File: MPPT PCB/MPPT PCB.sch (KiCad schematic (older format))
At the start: 26 parts, among them J1 Conn_01x03_Male, J10 Conn_01x03_Male, J11 Conn_01x03_Male, J12 Conn_01x03_Male, J13 Conn_01x03_Male, J2 Conn_01x03_Male, J3 Conn_01x06_Female, J4 Conn_01x03_Male, J5 Screw_Terminal_01x02, J6 Conn_01x03_Male, J7 Conn_01x03_Male, J8 Screw_Terminal_01x02, J9 Conn_01x06_Female, P1 Conn_01x15_Female, P2 Conn_01x15_Female, SW1 SW_Push

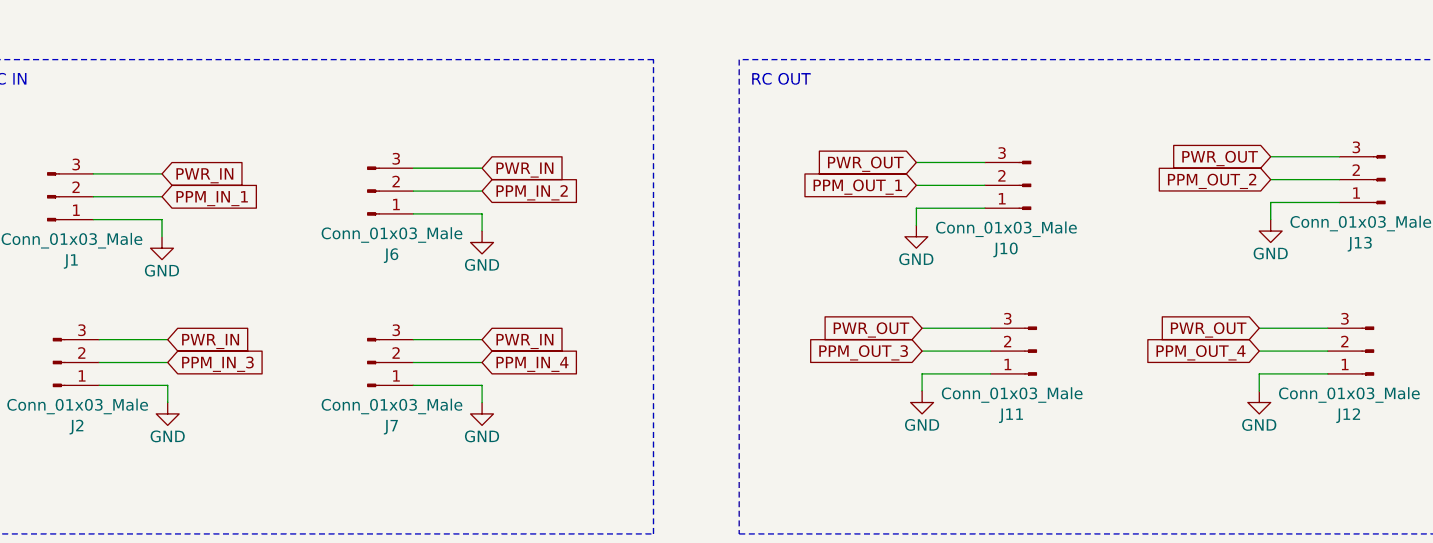
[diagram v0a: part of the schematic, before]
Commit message: Fixed servo pinout (Input and Output)
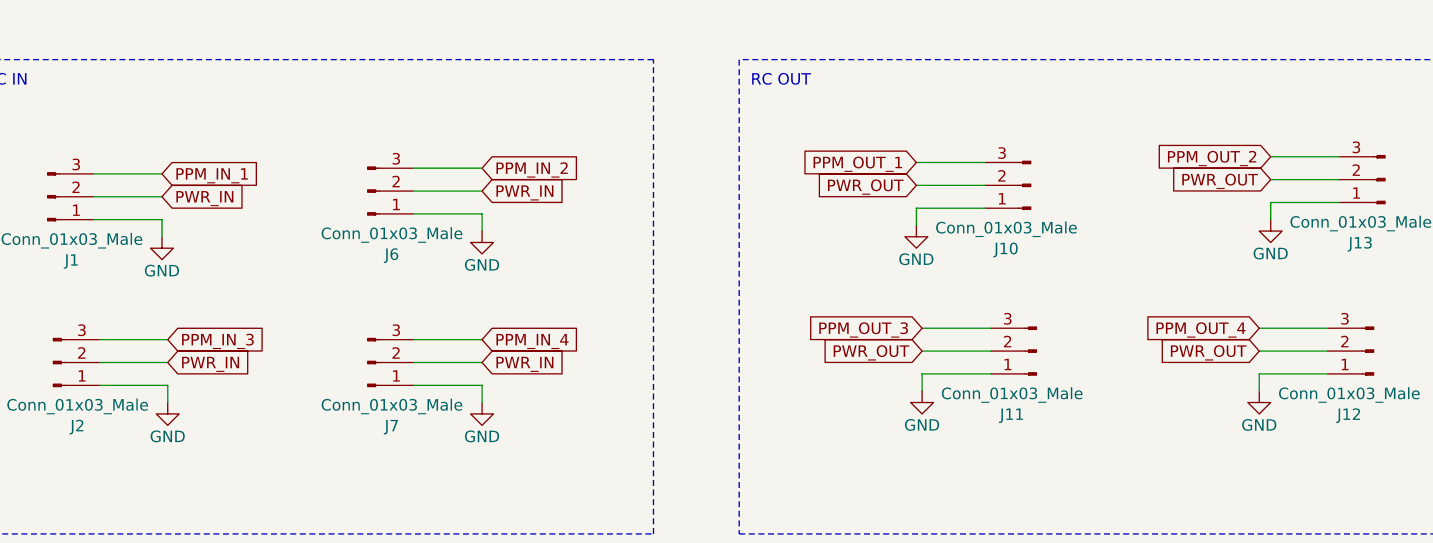
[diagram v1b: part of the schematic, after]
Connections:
- net PPM_IN_1: now also J1.3 (Pin_3); no longer J1.2 (Pin_2)
- net PPM_IN_2: now also J6.3 (Pin_3); no longer J6.2 (Pin_2)
- net PPM_IN_3: now also J2.3 (Pin_3); no longer J2.2 (Pin_2)
- net PPM_IN_4: now also J7.3 (Pin_3); no longer J7.2 (Pin_2)
- net PPM_OUT_1: now also J10.3 (Pin_3); no longer J10.2 (Pin_2)
- net PPM_OUT_2: now also J13.3 (Pin_3); no longer J13.2 (Pin_2)
- net PPM_OUT_3: now also J11.3 (Pin_3); no longer J11.2 (Pin_2)
- net PPM_OUT_4: now also J12.3 (Pin_3); no longer J12.2 (Pin_2)
- net PWR_IN: now also J1.2 (Pin_2), J2.2 (Pin_2), J6.2 (Pin_2), J7.2 (Pin_2); no longer J1.3 (Pin_3), J2.3 (Pin_3), J6.3 (Pin_3), J7.3 (Pin_3)
- net PWR_OUT: now also J10.2 (Pin_2), J11.2 (Pin_2), J12.2 (Pin_2), J13.2 (Pin_2); no longer J10.3 (Pin_3), J11.3 (Pin_3), J12.3 (Pin_3), J13.3 (Pin_3)
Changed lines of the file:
@@
 Title "MPPT solar board"
 Date "2019-10-12"
-Rev "r1"
+Rev "r2"
 Comp "Luis Miranda"
 Comment1 ""
@@
 	1    0    0    -1
 $EndComp
+Text GLabel 1650 1150 2    50   Input ~ 0
+PPM_IN_1
+Wire Wire Line
+	1650 1425 1650 1350
+Wire Wire Line
+	1650 1350 1350 1350
+Wire Wire Line
+	1650 1250 1350 1250
 Text GLabel 1650 1250 2    50   Input ~ 0
-PPM_IN_1
-Wire Wire Line
-	1650 1425 1650 1350
-Wire Wire Line
-	1650 1350 1350 1350
-Wire Wire Line
-	1650 1250 1350 1250
-Text GLabel 1650 1150 2    50   Input ~ 0
 PWR_IN
 Wire Wire Line
@@
 	1    0    0    -1
 $EndComp
+Text GLabel 1675 1875 2    50   Input ~ 0
+PPM_IN_3
+Wire Wire Line
+	1675 2150 1675 2075
+Wire Wire Line
+	1675 2075 1375 2075
+Wire Wire Line
+	1675 1975 1375 1975
 Text GLabel 1675 1975 2    50   Input ~ 0
-PPM_IN_3
-Wire Wire Line
-	1675 2150 1675 2075
-Wire Wire Line
-	1675 2075 1375 2075
-Wire Wire Line
-	1675 1975 1375 1975
-Text GLabel 1675 1875 2    50   Input ~ 0
 PWR_IN
 Wire Wire Line
@@
 	1    0    0    -1
 $EndComp
+Text GLabel 3050 1125 2    50   Input ~ 0
+PPM_IN_2
+Wire Wire Line
+	3050 1400 3050 1325
+Wire Wire Line
+	3050 1325 2750 1325
+Wire Wire Line
+	3050 1225 2750 1225
 Text GLabel 3050 1225 2    50   Input ~ 0
-PPM_IN_2
-Wire Wire Line
-	3050 1400 3050 1325
-Wire Wire Line
-	3050 1325 2750 1325
-Wire Wire Line
-	3050 1225 2750 1225
-Text GLabel 3050 1125 2    50   Input ~ 0
 PWR_IN
 Wire Wire Line
@@
 	1    0    0    -1
 $EndComp
+Text GLabel 3050 1875 2    50   Input ~ 0
+PPM_IN_4
+Wire Wire Line
+	3050 2150 3050 2075
+Wire Wire Line
+	3050 2075 2750 2075
+Wire Wire Line
+	3050 1975 2750 1975
 Text GLabel 3050 1975 2    50   Input ~ 0
-PPM_IN_4
-Wire Wire Line
-	3050 2150 3050 2075
-Wire Wire Line
-	3050 2075 2750 2075
-Wire Wire Line
-	3050 1975 2750 1975
-Text GLabel 3050 1875 2    50   Input ~ 0
 PWR_IN
 Wire Wire Line
@@
 	-1   0    0    -1
 $EndComp
+Text GLabel 4950 1100 0    50   Input ~ 0
+PPM_OUT_1
+Wire Wire Line
+	4950 1375 4950 1300
+Wire Wire Line
+	4950 1300 5250 1300
+Wire Wire Line
+	4950 1200 5250 1200
 Text GLabel 4950 1200 0    50   Input ~ 0
-PPM_OUT_1
-Wire Wire Line
-	4950 1375 4950 1300
-Wire Wire Line
-	4950 1300 5250 1300
-Wire Wire Line
-	4950 1200 5250 1200
-Text GLabel 4950 1100 0    50   Input ~ 0
 PWR_OUT
 Wire Wire Line
@@
 	-1   0    0    -1
 $EndComp
+Text GLabel 4975 1825 0    50   Input ~ 0
+PPM_OUT_3
+Wire Wire Line
+	4975 2100 4975 2025
+Wire Wire Line
+	4975 2025 5275 2025
+Wire Wire Line
+	4975 1925 5275 1925
 Text GLabel 4975 1925 0    50   Input ~ 0
-PPM_OUT_3
-Wire Wire Line
-	4975 2100 4975 2025
-Wire Wire Line
-	4975 2025 5275 2025
-Wire Wire Line
-	4975 1925 5275 1925
-Text GLabel 4975 1825 0    50   Input ~ 0
 PWR_OUT
 Wire Wire Line
@@
 	-1   0    0    -1
 $EndComp
+Text GLabel 6500 1075 0    50   Input ~ 0
+PPM_OUT_2
+Wire Wire Line
+	6500 1350 6500 1275
+Wire Wire Line
+	6500 1275 6800 1275
+Wire Wire Line
+	6500 1175 6800 1175
 Text GLabel 6500 1175 0    50   Input ~ 0
-PPM_OUT_2
-Wire Wire Line
-	6500 1350 6500 1275
-Wire Wire Line
-	6500 1275 6800 1275
-Wire Wire Line
-	6500 1175 6800 1175
-Text GLabel 6500 1075 0    50   Input ~ 0
 PWR_OUT
 Wire Wire Line
@@
 	-1   0    0    -1
 $EndComp
+Text GLabel 6450 1825 0    50   Input ~ 0
+PPM_OUT_4
+Wire Wire Line
+	6450 2100 6450 2025
+Wire Wire Line
+	6450 2025 6750 2025
+Wire Wire Line
+	6450 1925 6750 1925
 Text GLabel 6450 1925 0    50   Input ~ 0
-PPM_OUT_4
-Wire Wire Line
-	6450 2100 6450 2025
-Wire Wire Line
-	6450 2025 6750 2025
-Wire Wire Line
-	6450 1925 6750 1925
-Text GLabel 6450 1825 0    50   Input ~ 0
 PWR_OUT
 Wire Wire Line

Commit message: Version 2 of PCB
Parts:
- added J14, J15, J16, J17: Conn_01x01_Male, digikey-footprints:Test_Point_2.67x1.02mm, symbol Connector:Conn_01x01_Male
- D1: value LED -> LED_G; DIGIKEY_PN (none) -> 732-5008-ND
- D2: value LED -> LED_O; DIGIKEY_PN (none) -> 732-5010-ND
- R3, R4: value 1K -> 150R; DIGIKEY_PN CF14JT1K00CT-ND -> CF14JT150RCT-ND
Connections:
- net +5V: now also J14.1 (Pin_1)
- net GND: now also J17.1 (Pin_1)
- net SCL: now also J16.1 (Pin_1)
- net SDA: now also J15.1 (Pin_1)
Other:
- note added: "I2C solder pads"
- moved on the sheet: C1, D1, D2, R3, R4, R5, SW1
